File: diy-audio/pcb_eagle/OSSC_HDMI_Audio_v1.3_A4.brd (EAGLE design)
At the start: 29.8 x 24 mm, 29 parts, among them U1 PCM1808, U2 74LVC1G34, U3 MK2507SLF

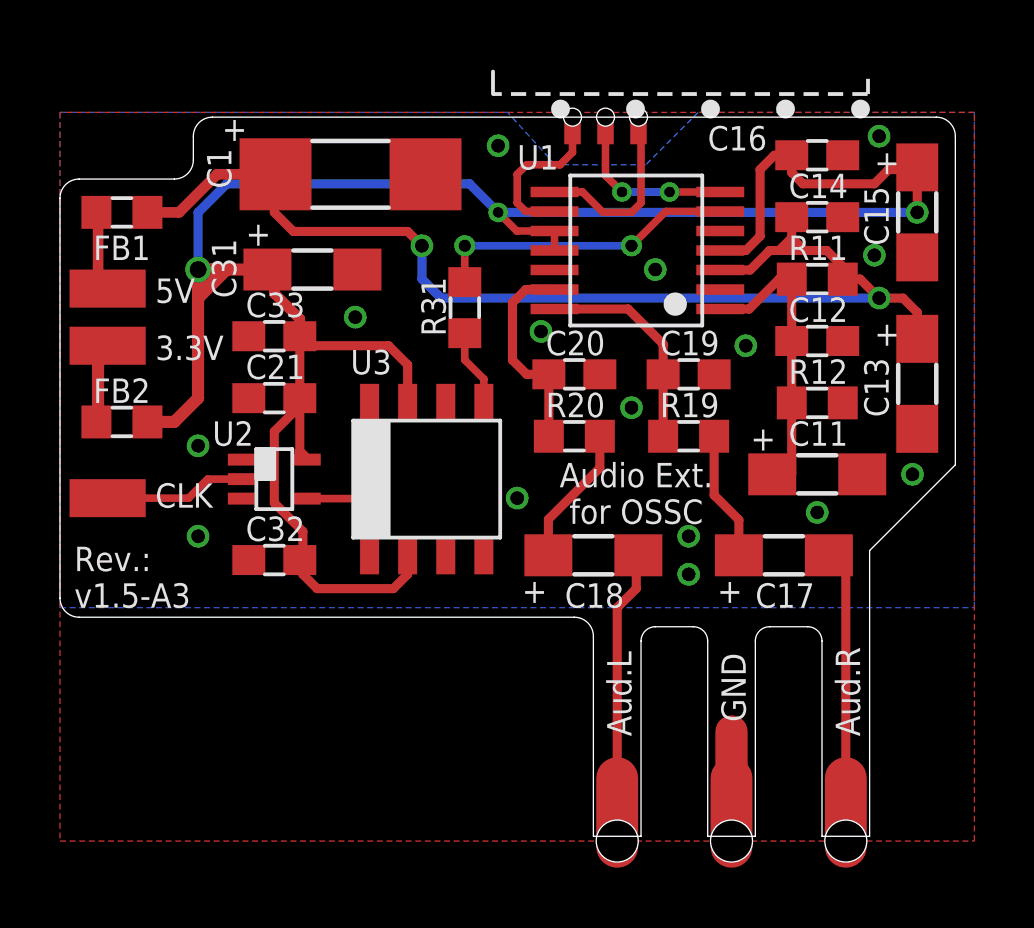
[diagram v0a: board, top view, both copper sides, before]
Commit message: PCB files with a pad for mclk to IT6613E
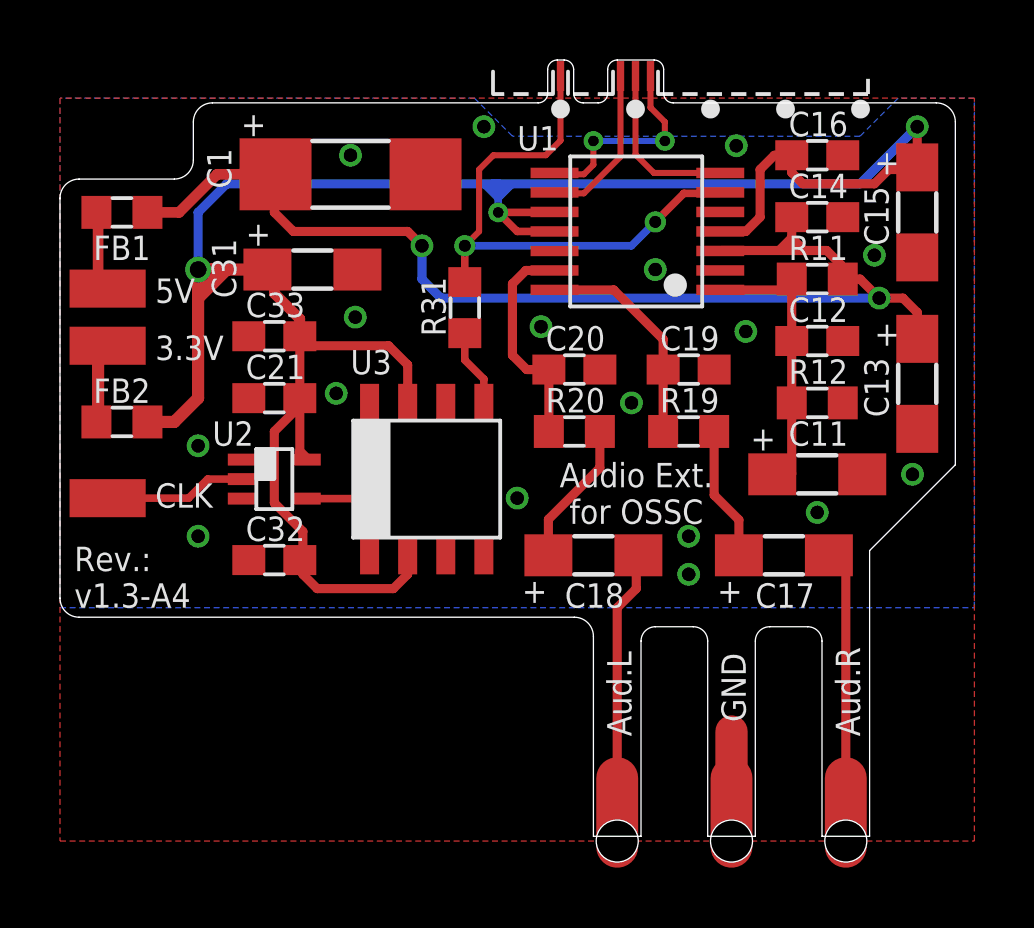
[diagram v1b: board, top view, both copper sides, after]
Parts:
- removed U$1: OSSC_DIY_AUDIO_OVERLAYDIY-V1.5, OSSC_HDMI_Audio:OSSC_OVERLAY_V1.5
- added U$4: OSSC_DIY_AUDIO_OVERLAYDIY-V1.3, OSSC_HDMI_Audio:OSSC_OVERLAY_V1.3
- moved U1 0.64 mm to (19.2, 20.3)
- moved C19 0.16 mm to (21.0, 15.7)
- moved C20 0.16 mm to (17.1, 15.7)
- moved R19 0.16 mm to (21.0, 13.7)
- moved R20 0.16 mm to (17.1, 13.7)
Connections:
- net GND: now also U$4.4; no longer U$1.4
- net N$1: now also U$4.6; no longer U$1.6
- net N$13: now also U$4.10; no longer U$1.10
- net N$14: now also U$4.11; no longer U$1.11
- net N$15: now also U$4.9; no longer U$1.9
- net N$17: now also U$4.5
- net N$2: now also U$4.2; no longer U$1.2
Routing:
- net N$17: track 10.2 -> 18.8 mm
- net VDD: track 75.2 -> 80.0 mm
- net N$14: track 5.81 -> 6.98 mm, vias 0 -> 2
- net N$13: track 5.62 -> 5.69 mm, vias 2 -> 0
- net GND: vias 15 -> 17
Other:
- board size 29.8 x 24 mm -> 29.8 x 25.9 mm
- board text added: "Rev.: v1.3-A4"
- board text removed: "Rev.: v1.5-A3"
